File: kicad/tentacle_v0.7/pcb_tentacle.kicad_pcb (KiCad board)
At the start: 2 copper layers, 100 x 165 mm, 955 parts, among them J1302 Conn_02x20, J1303 Conn_02x20, J1501 Conn_02x20, J1502 Conn_01x12, J201 Conn_02x05, J202 Conn_01x5, J301 USB_C_Receptacle_USB2.0, J501 Conn_02x20, U1001 GAQY221S, U1101 GAQY221S, U1201 GAQY221S, U1501 RP2040, U1502 W25Q32JVS, U1503 TXB0108PW, U1504 TXB0108PW, U201 RP2040, U202 AMS1117-3.3, U203 W25Q32JVS, U204 TPS2595xx, U205 TPS2595xx, U207 TPS2595xx, U302 USB2514B_Bi, U601 GAQY221S, U701 GAQY221S, U801 GAQY221S, U901 GAQY221S, X201 Oscillator-12MHz, Y301 24MHz

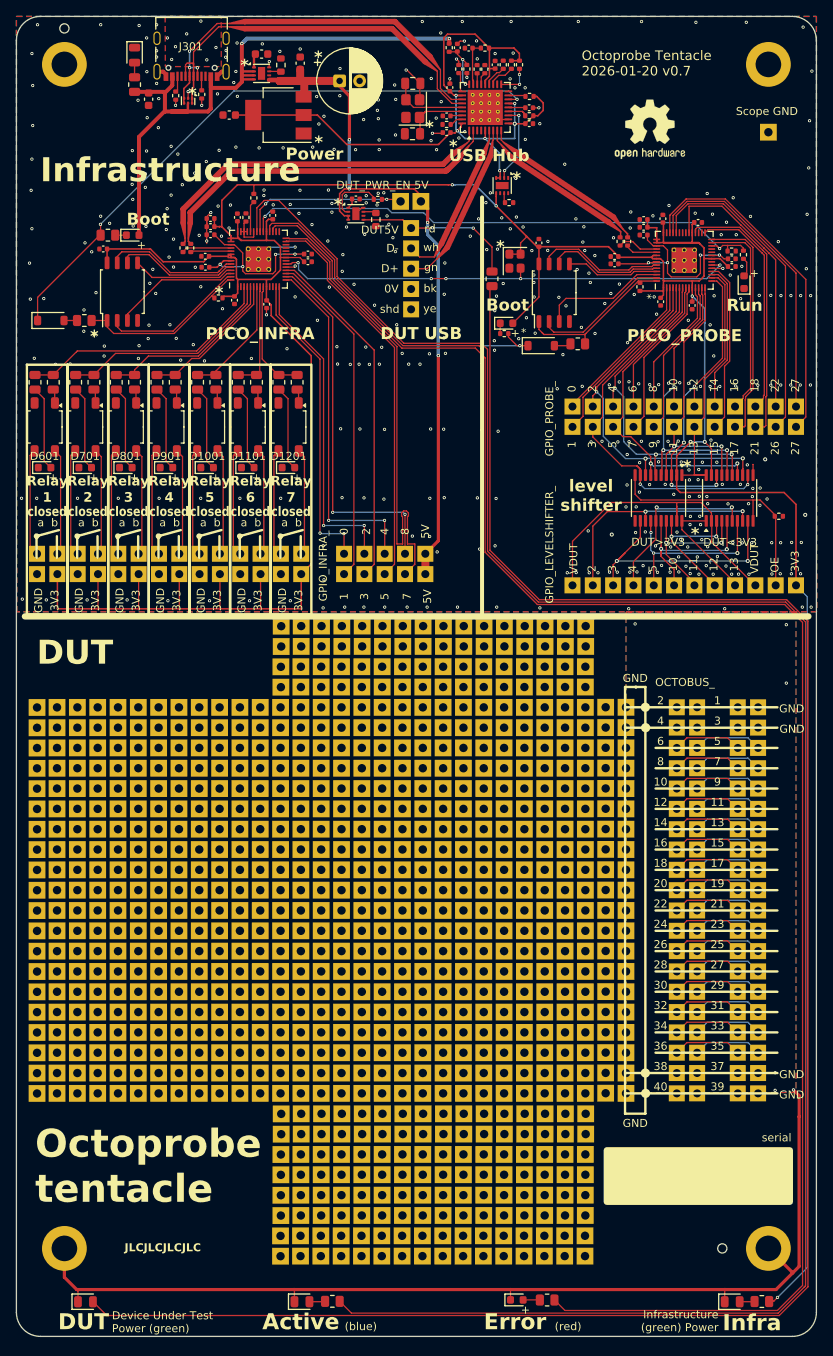
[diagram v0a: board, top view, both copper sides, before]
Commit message: Tentacle v0.7: Fix LEDs. Import new symbols and footprints
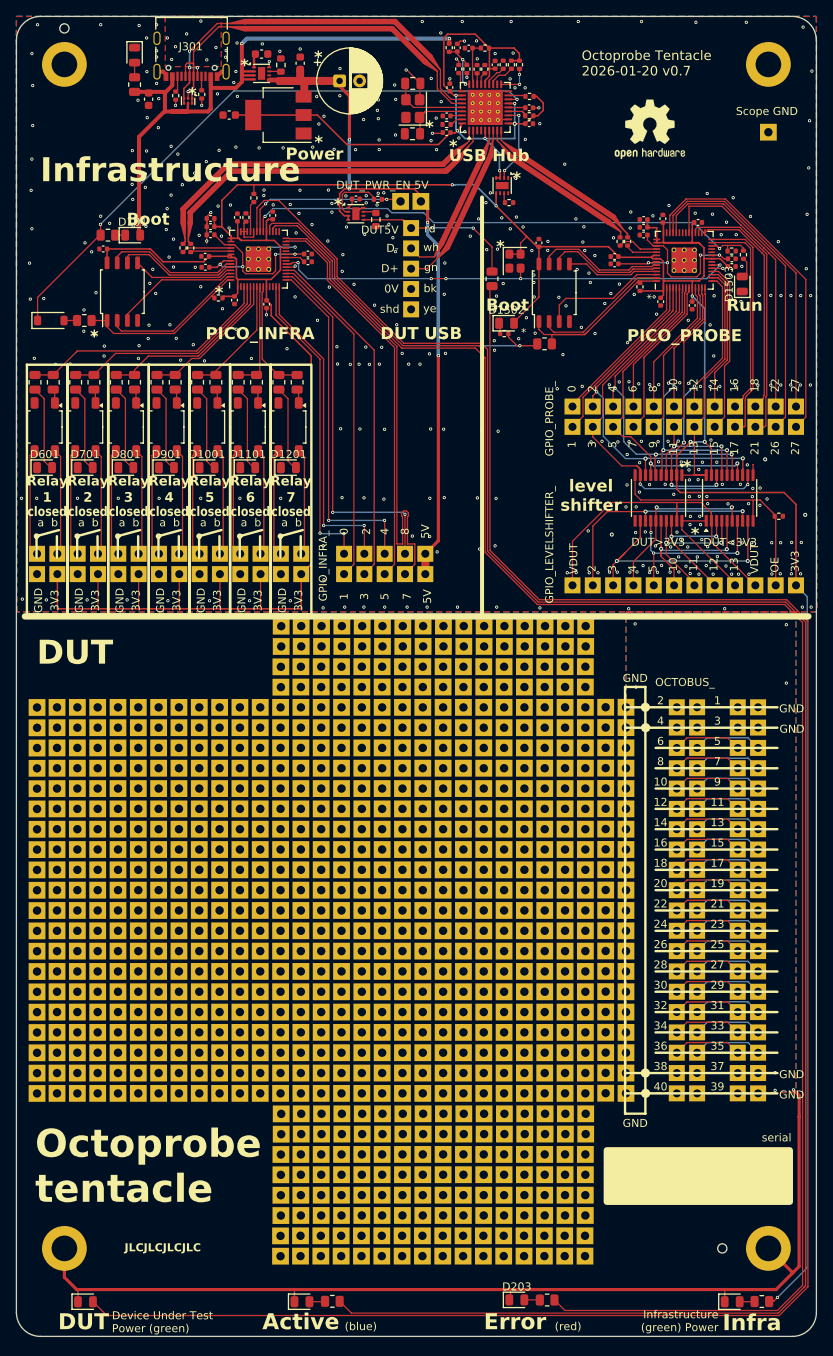
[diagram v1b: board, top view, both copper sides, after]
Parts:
- removed D1501: B5819W SL, Diode_SMD:D_SOD-123
- D1001, D101, D1101, D1201, D1502, D1503, D203, D601, D701, D801, D901: footprint 00_project_library:LED_0603_1608Metric -> LED_SMD:LED_0805_2012Metric
- R1503: value 0R -> 1k
- moved R1503 4.15 mm to (124.8, 58.2)
- moved D1503 0.32 mm to (149.5, 50.7)
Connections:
- R1503 pad 2: Net-(D1501-A) -> RP2_PROBE_BOOT
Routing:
- net /RP2 PROBE/QSPI_SS: track 20.4 -> 24.6 mm
- net Net-(D1501-A): track 1.78 -> 0.00 mm
- net +5Vbuf: track 95.6 -> 94.4 mm
- net RP2_PROBE_BOOT: track 43.4 -> 44.3 mm

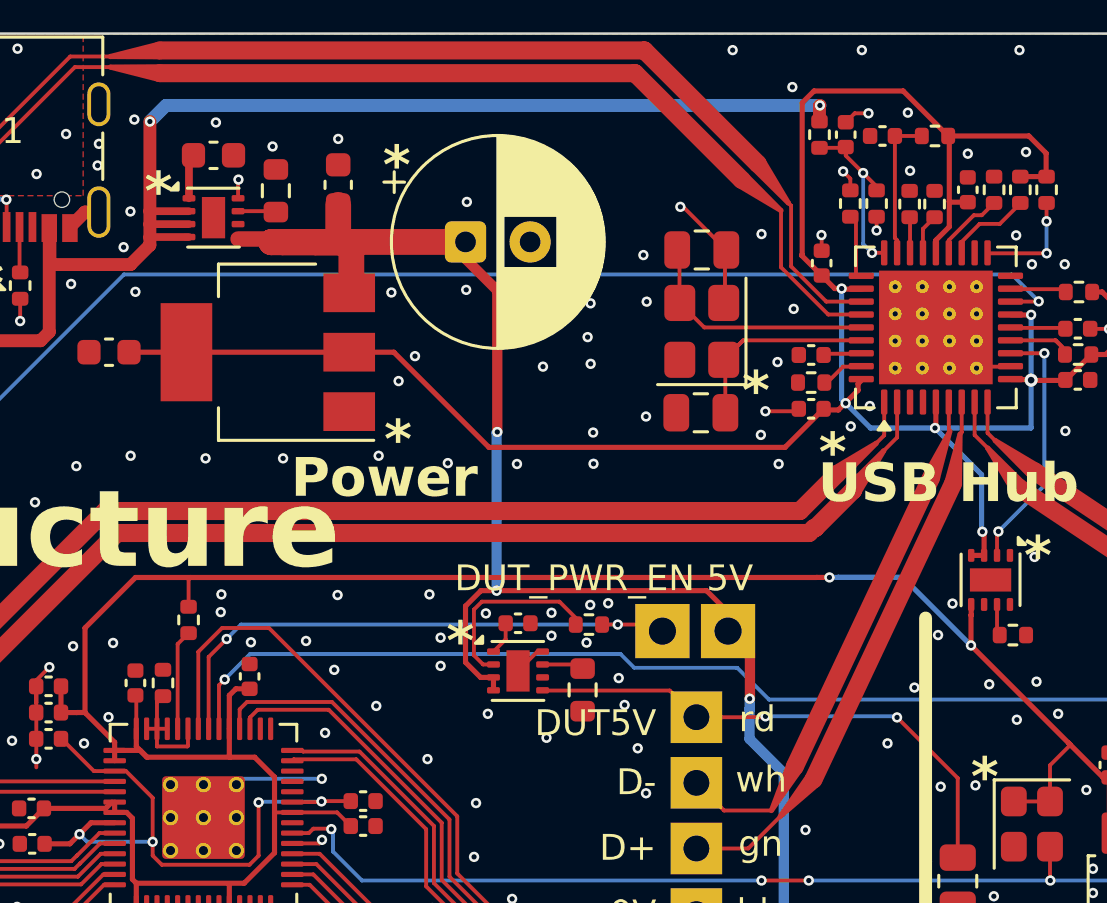
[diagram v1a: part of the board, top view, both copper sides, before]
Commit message: Tentacle v0.7: HUB U302: CFG_SEL_1 0->1
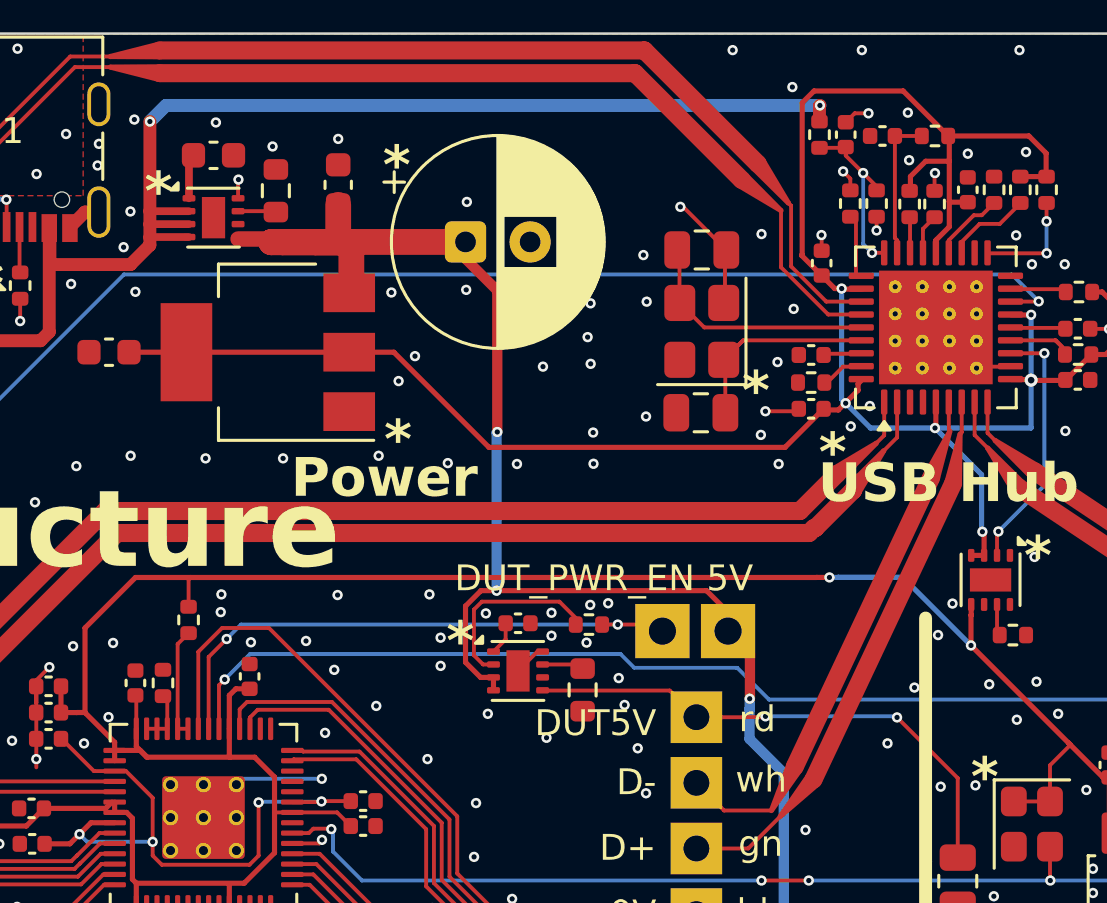
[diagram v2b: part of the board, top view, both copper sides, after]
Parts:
- R311: value 100k -> 10k
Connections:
- R210 pad 1: Net-(U201-GPIO25) -> Net-(U201-GPIO27/ADC1)
- R213 pad 1: Net-(U201-GPIO26/ADC0) -> Net-(U201-GPIO25)
- R311 pad 1: GND -> +3V3
- U201 pad 38: Net-(U201-GPIO26/ADC0) -> Net-(U201-GPIO25)
- U201 pad 39: Net-(U201-GPIO25) -> Net-(U201-GPIO27/ADC1)
- U201 pad 40: Net-(U201-GPIO25) -> Net-(U201-GPIO27/ADC1)
- U201 pad 41: Net-(U201-GPIO25) -> Net-(U201-GPIO27/ADC1)
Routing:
- net Net-(U201-GPIO26/ADC0): track 3.88 -> 0.00 mm
- net +3V3: track 89.6 -> 91.9 mm
- net Net-(U201-GPIO27/ADC1): track 0.00 -> 1.90 mm
- net GND: track 160.6 -> 161.3 mm, vias 467 -> 468
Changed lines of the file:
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@@
 	(net 51 "Net-(U201-GPIO25)")
 	(net 52 "RP2_PROBE_RUN")
-	(net 53 "Net-(U201-GPIO26{slash}ADC0)")
+	(net 53 "Net-(U201-GPIO27{slash}ADC1)")
 	(net 54 "Net-(J1302-Pin_25)")
 	(net 55 "Net-(U204-dV{slash}dT)")
@@
 			(layers "F.Cu" "F.Mask" "F.Paste")
 			(roundrect_rratio 0.25)
-			(net 53 "Net-(U201-GPIO26{slash}ADC0)")
+			(net 51 "Net-(U201-GPIO25)")
 			(pintype "passive")
 		)
@@
 			)
 		)
-		(property "Value" "100k"
+		(property "Value" "10k"
 			(at 0 1.17 90)
 			(layer "F.Fab")
@@
 			(layers "F.Cu" "F.Mask" "F.Paste")
 			(roundrect_rratio 0.25)
-			(net 5 "GND")
+			(net 12 "+3V3")
 			(pintype "passive")
 		)
@@
 			(layers "F.Cu" "F.Mask" "F.Paste")
 			(roundrect_rratio 0.25)
-			(net 53 "Net-(U201-GPIO26{slash}ADC0)")
+			(net 51 "Net-(U201-GPIO25)")
 			(pinfunction "GPIO26/ADC0")
 			(pintype "bidirectional")
@@
 			(layers "F.Cu" "F.Mask" "F.Paste")
 			(roundrect_rratio 0.25)
-			(net 51 "Net-(U201-GPIO25)")
+			(net 53 "Net-(U201-GPIO27{slash}ADC1)")
 			(pinfunction "GPIO27/ADC1")
 			(pintype "bidirectional")
@@
 			(layers "F.Cu" "F.Mask" "F.Paste")
 			(roundrect_rratio 0.25)
-			(net 51 "Net-(U201-GPIO25)")
+			(net 53 "Net-(U201-GPIO27{slash}ADC1)")
 			(pinfunction "GPIO28/ADC2")
 			(pintype "bidirectional")
@@
 			(layers "F.Cu" "F.Mask" "F.Paste")
 			(roundrect_rratio 0.25)
-			(net 51 "Net-(U201-GPIO25)")
+			(net 53 "Net-(U201-GPIO27{slash}ADC1)")
 			(pinfunction "GPIO29/ADC3")
 			(pintype "bidirectional")
@@
 			(layers "F.Cu" "F.Mask" "F.Paste")
 			(roundrect_rratio 0.25)
-			(net 51 "Net-(U201-GPIO25)")
+			(net 53 "Net-(U201-GPIO27{slash}ADC1)")
 			(pintype "passive")
 		)
@@
 	)
 	(segment
+		(start 117.3142 23.3472)
+		(end 117.3142 22.6758)
+		(width 0.15)
+		(layer "F.Cu")
+		(net 5)
+	)
+	(segment
 		(start 66.4585 177.923)
 		(end 66.4585 176.5675)
@@
 	)
 	(via
-		(at 116.3658 22.5686)
+		(at 116.33 22.16)
 		(size 0.4)
 		(drill 0.2)
@@
 	)
 	(via
+		(at 117.33 22.66)
+		(size 0.4)
+		(drill 0.2)
+		(layers "F.Cu" "B.Cu")
+		(free yes)
+		(net 5)
+	)
+	(via
 		(at 115.4938 44.7294)
 		(size 0.4)
@@
 	)
 	(segment
+		(start 116.97 22.2)
+		(end 116.38 22.79)
+		(width 0.2)
+		(layer "F.Cu")
+		(net 12)
+	)
+	(segment
 		(start 123.9386 29.6806)
 		(end 123.3812 29.6806)
@@
 	)
 	(segment
+		(start 116.38 22.79)
+		(end 116.38 23.3162)
+		(width 0.2)
+		(layer "F.Cu")
+		(net 12)
+	)
+	(segment
 		(start 117.365 25.257401)
 		(end 117.8842 24.738201)
@@
 	)
 	(segment
+		(start 117.8842 22.2)
+		(end 116.97 22.2)
+		(width 0.2)
+		(layer "F.Cu")
+		(net 12)
+	)
+	(segment
 		(start 117.365 32.4914)
 		(end 117.331 32.5254)
@@
 	)
 	(segment
-		(start 86.8195 44.165)
-		(end 87.6195 44.165)
-		(width 0.15)
-		(layer "F.Cu")
-		(net 51)
-	)
-	(segment
-		(start 87.2195 43.1333)
-		(end 87.2195 44.165)
+		(start 88.0195 40.8875)
+		(end 88.4428 40.4642)
 		(width 0.15)
 		(layer "F.Cu")
@@
 	)
 	(segment
-		(start 88.4195 44.8267)
+		(start 88.0195 44.165)
 		(end 88.4195 44.165)
 		(width 0.15)
@@
 	)
 	(segment
-		(start 88.3967 44.8495)
-		(end 88.4195 44.8267)
-		(width 0.15)
-		(layer "F.Cu")
-		(net 51)
-	)
-	(segment
-		(start 87.4502 42.9026)
-		(end 87.2195 43.1333)
-		(width 0.15)
-		(layer "F.Cu")
-		(net 51)
-	)
-	(segment
-		(start 87.2195 44.8495)
-		(end 88.3967 44.8495)
-		(width 0.15)
-		(layer "F.Cu")
-		(net 51)
-	)
-	(segment
-		(start 87.2195 44.165)
-		(end 87.2195 44.8495)
+		(start 88.0195 44.165)
+		(end 88.0195 40.8875)
 		(width 0.15)
 		(layer "F.Cu")
@@
 	)
 	(segment
-		(start 88.0195 40.8875)
-		(end 88.4428 40.4642)
+		(start 86.8195 44.165)
+		(end 87.6195 44.165)
 		(width 0.15)
 		(layer "F.Cu")
@@
 	)
 	(segment
-		(start 88.0195 44.165)
-		(end 88.0195 40.8875)
+		(start 87.6195 44.165)
+		(end 87.6195 43.0699)
 		(width 0.15)
 		(layer "F.Cu")

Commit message: Tentacle: v0.7
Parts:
- added BP220: USB_PROBE_D-, 00_project_library:octoprobe_breakout_PB, F.Cu at (129.3, 44.6)
- added BP221: USB_PROBE_D+, 00_project_library:octoprobe_breakout_PB, F.Cu at (135.4, 39.8)
- added BP222: USB_PROBE_PWR, 00_project_library:octoprobe_breakout_PB, F.Cu at (140.5, 39.8)
- added BP223: USB_PROBE_5V, 00_project_library:octoprobe_breakout_PB, F.Cu at (126.8, 44.6)
- added BP224: USB_PROBE_GND, 00_project_library:octoprobe_breakout_PB, F.Cu at (138.0, 39.8)
- added R220: 0R, Resistor_SMD:R_0603_1608Metric, F.Cu at (134.6, 45.3)
- added R221: 0R, Resistor_SMD:R_0603_1608Metric, F.Cu at (134.6, 46.8)
- moved R1502 3.02 mm to (137.2, 46.1), turned to 0 degrees
- moved R1501 2.58 mm to (137.1, 47.0), turned to 0 degrees
- moved C1502 1.75 mm to (131.8, 48.4)
- moved C1505 1.75 mm to (131.8, 47.4)
- moved C1507 0.32 mm to (124.1, 45.9)
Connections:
- NT102 pad 1: _USB_PROBE_D- -> Net-(BP220-Pad1)
- NT102 pad 3: _USB_PROBE_D+ -> Net-(BP221-Pad1)
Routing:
- net /USB Hub Chip/PRT_PWR4: track 0.00 -> 29.1 mm
- net +5Vbuf: track 94.4 -> 113.0 mm, vias 4 -> 6
- net Net-(BP221-Pad1): track 0.00 -> 7.80 mm
- net Net-(BP220-Pad1): track 0.00 -> 5.05 mm
- net Net-(U1501-USB-DM): track 5.13 -> 1.24 mm
- net Net-(U1501-USB-DP): track 3.92 -> 1.28 mm
- net /RP2 PROBE/+1V1: track 25.2 -> 27.1 mm
- net /RP2 PROBE/GPIO22: track 35.3 -> 34.0 mm
- net /RP2 PROBE/GPIO26: track 40.3 -> 39.0 mm
- net /RP2 PROBE/GPIO27: track 38.7 -> 37.5 mm
- net /RP2 PROBE/GPIO28: track 43.1 -> 41.9 mm
- net _USB_PROBE_D-: track 0.70 -> 1.56 mm
- net GND: vias 468 -> 477
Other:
- board text added: "0V"
- board text added: "D+"
- board text added: "D-"
- board text added: "R209"
- board text added: "pwr"
